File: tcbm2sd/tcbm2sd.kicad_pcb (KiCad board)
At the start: 2 copper layers, 56 x 91 mm, 13 parts, among them J2 JTAG, J3 debug, J4 AMS1117, J5 SD CARD, J7 debug, J8 C16-Exp-Port, U1 XC9572XL-VQ64, U2 Arduino_Pro_Mini

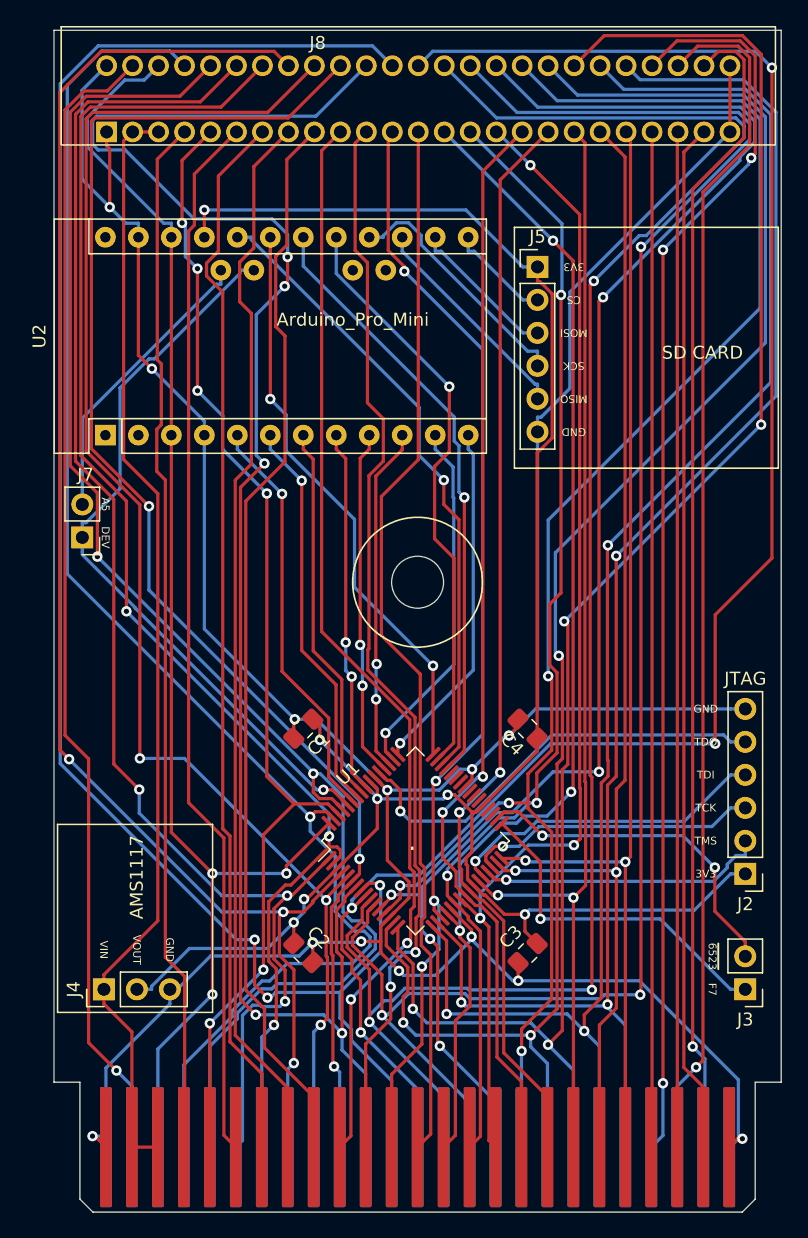
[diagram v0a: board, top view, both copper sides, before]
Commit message: fabrication files for v1.0 development board with Arduino, SD card module and AMS1117 power module
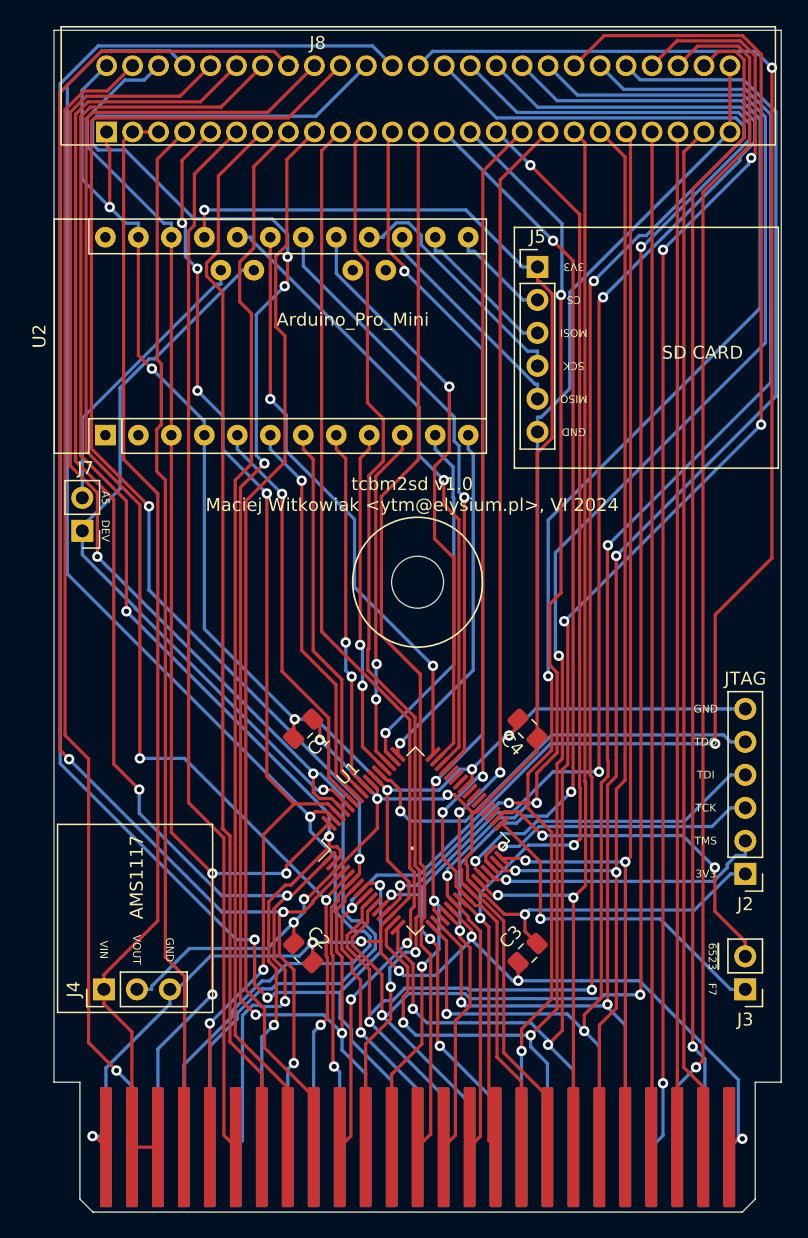
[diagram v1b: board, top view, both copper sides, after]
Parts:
- moved J7 0.51 mm to (122.7, 98.0)
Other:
- board text added: "tcbm2sd v1.0 Maciej Witkowiak <ytm@elysium.pl>, VI 2024"
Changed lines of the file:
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@@
       (layerselection 0x00010fc_ffffffff)
       (disableapertmacros false)
-      (usegerberextensions false)
-      (usegerberattributes true)
-      (usegerberadvancedattributes true)
-      (creategerberjobfile true)
+      (usegerberextensions true)
+      (usegerberattributes false)
+      (usegerberadvancedattributes false)
+      (creategerberjobfile false)
       (svguseinch false)
       (svgprecision 6)
@@
       (plotinvisibletext false)
       (sketchpadsonfab false)
-      (subtractmaskfromsilk false)
+      (subtractmaskfromsilk true)
       (outputformat 1)
       (mirror false)
-      (drillshape 1)
+      (drillshape 0)
       (scaleselection 1)
-      (outputdirectory "")
+      (outputdirectory "plots/")
     )
   )
@@
     (fp_line (start 1 -0.625) (end 1 0.625) (layer "F.Fab") (width 0.1))
     (fp_line (start -1 -0.625) (end 1 -0.625) (layer "F.Fab") (width 0.1))
-    (pad "1" smd roundrect (at -1.0375 0 225) (size 1.175 1.45) (layers "F.Cu" "F.Paste" "F.Mask") (roundrect_rratio 0.212766)
+    (pad "1" smd roundrect (at -1.0375 0 225) (size 1.175 1.45) (layers "F.Cu" "F.Paste" "F.Mask") (roundrect_rratio 0.2127659574)
       (net 50 "+3V3") (pintype "passive"))
-    (pad "2" smd roundrect (at 1.0375 0 225) (size 1.175 1.45) (layers "F.Cu" "F.Paste" "F.Mask") (roundrect_rratio 0.212766)
+    (pad "2" smd roundrect (at 1.0375 0 225) (size 1.175 1.45) (layers "F.Cu" "F.Paste" "F.Mask") (roundrect_rratio 0.2127659574)
       (net 17 "GND") (pintype "passive"))
     (model "${KICAD6_3DMODEL_DIR}/Capacitor_SMD.3dshapes/C_0805_2012Metric.wrl"
@@
     (fp_line (start 1 0.625) (end -1 0.625) (layer "F.Fab") (width 0.1))
     (fp_line (start 1 -0.625) (end 1 0.625) (layer "F.Fab") (width 0.1))
-    (pad "1" smd roundrect (at -1.0375 0 135) (size 1.175 1.45) (layers "F.Cu" "F.Paste" "F.Mask") (roundrect_rratio 0.212766)
+    (pad "1" smd roundrect (at -1.0375 0 135) (size 1.175 1.45) (layers "F.Cu" "F.Paste" "F.Mask") (roundrect_rratio 0.2127659574)
       (net 50 "+3V3") (pintype "passive"))
-    (pad "2" smd roundrect (at 1.0375 0 135) (size 1.175 1.45) (layers "F.Cu" "F.Paste" "F.Mask") (roundrect_rratio 0.212766)
+    (pad "2" smd roundrect (at 1.0375 0 135) (size 1.175 1.45) (layers "F.Cu" "F.Paste" "F.Mask") (roundrect_rratio 0.2127659574)
       (net 17 "GND") (pintype "passive"))
     (model "${KICAD6_3DMODEL_DIR}/Capacitor_SMD.3dshapes/C_0805_2012Metric.wrl"
@@
     (fp_line (start -1 0.625) (end -1 -0.625) (layer "F.Fab") (width 0.1))
     (fp_line (start 1 -0.625) (end 1 0.625) (layer "F.Fab") (width 0.1))
-    (pad "1" smd roundrect (at -1.0375 0 315) (size 1.175 1.45) (layers "F.Cu" "F.Paste" "F.Mask") (roundrect_rratio 0.212766)
+    (pad "1" smd roundrect (at -1.0375 0 315) (size 1.175 1.45) (layers "F.Cu" "F.Paste" "F.Mask") (roundrect_rratio 0.2127659574)
       (net 50 "+3V3") (pintype "passive"))
-    (pad "2" smd roundrect (at 1.0375 0 315) (size 1.175 1.45) (layers "F.Cu" "F.Paste" "F.Mask") (roundrect_rratio 0.212766)
+    (pad "2" smd roundrect (at 1.0375 0 315) (size 1.175 1.45) (layers "F.Cu" "F.Paste" "F.Mask") (roundrect_rratio 0.2127659574)
       (net 17 "GND") (pintype "passive"))
     (model "${KICAD6_3DMODEL_DIR}/Capacitor_SMD.3dshapes/C_0805_2012Metric.wrl"
@@
   )
   (footprint "Connector_PinHeader_2.54mm:PinHeader_1x02_P2.54mm_Vertical" (layer "F.Cu")
-    (at 122.682 98.552 180)
+    (at 122.682 98.044 180)
     (descr "Through hole straight pin header, 1x02, 2.54mm pitch, single row")
     (tags "Through hole pin header THT 1x02 2.54mm single row")
@@
     (fp_line (start -1 0.625) (end -1 -0.625) (layer "F.Fab") (width 0.1))
     (fp_line (start 1 -0.625) (end 1 0.625) (layer "F.Fab") (width 0.1))
-    (pad "1" smd roundrect (at -1.0375 0 225) (size 1.175 1.45) (layers "F.Cu" "F.Paste" "F.Mask") (roundrect_rratio 0.212766)
+    (pad "1" smd roundrect (at -1.0375 0 225) (size 1.175 1.45) (layers "F.Cu" "F.Paste" "F.Mask") (roundrect_rratio 0.2127659574)
       (net 50 "+3V3") (pintype "passive"))
-    (pad "2" smd roundrect (at 1.0375 0 225) (size 1.175 1.45) (layers "F.Cu" "F.Paste" "F.Mask") (roundrect_rratio 0.212766)
+    (pad "2" smd roundrect (at 1.0375 0 225) (size 1.175 1.45) (layers "F.Cu" "F.Paste" "F.Mask") (roundrect_rratio 0.2127659574)
       (net 17 "GND") (pintype "passive"))
     (model "${KICAD6_3DMODEL_DIR}/Capacitor_SMD.3dshapes/C_0805_2012Metric.wrl"
@@
     (effects (font (size 0.6 0.6) (thickness 0.15)))
   )
+  (gr_text "tcbm2sd v1.0\nMaciej Witkowiak <ytm@elysium.pl>, VI 2024" (at 148.082 95.25) (layer "F.SilkS")
+    (effects (font (size 1 1) (thickness 0.15)))
+  )
   (gr_text "3V3" (at 170.688 124.46) (layer "F.SilkS")
     (effects (font (size 0.6 0.6) (thickness 0.15)))
@@
     (effects (font (size 0.6 0.6) (thickness 0.15)))
   )
-  (gr_text "A5" (at 124.46 96.007 270) (layer "F.SilkS")
+  (gr_text "A5" (at 124.46 95.499 270) (layer "F.SilkS")
     (effects (font (size 0.6 0.6) (thickness 0.15)))
   )
@@
     (effects (font (size 0.6 0.6) (thickness 0.15)))
   )
-  (gr_text "DEV" (at 124.46 98.547 270) (layer "F.SilkS")
+  (gr_text "DEV" (at 124.46 98.039 270) (layer "F.SilkS")
     (effects (font (size 0.6 0.6) (thickness 0.15)))
   )
@@
   (group "" (id 6a806a18-c268-401e-8a5b-6e7f55ce3bb1)
     (members
+      31c1165e-a0bf-4c0c-8b22-53e4006f1e7d
       486932fb-7172-4776-b2f5-f34e65d16cc5
       7e72e076-b042-46ad-b632-cac52bee2d82
